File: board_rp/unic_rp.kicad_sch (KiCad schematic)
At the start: 193 parts, among them J1 SM03B-SRSS-TB, P1 USB_C_Plug_USB2.0, Q1 2N7002, Q10 2N7002, Q11 2N7002, Q12 2N7002, Q13 2N7002, Q14 2N7002, Q15 2N7002, Q16 2N7002, Q17 2N7002, Q18 2N7002, Q19 2N7002, Q2 2N7002, Q20 2N7002, Q21 2N7002, Q22 2N7002, Q23 2N7002, Q24 2N7002, Q25 2N7002, Q26 2N7002, Q27 2N7002, Q28 2N7002, Q29 2N7002, Q3 2N7002, Q30 2N7002, Q31 2N7002, Q32 2N7002, Q33 2N7002, Q34 2N7002, Q35 2N7002, Q36 2N7002, Q37 2N7002, Q38 2N7002, Q39 2N7002, Q4 2N7002, Q40 2N7002, Q41 2N7002, Q5 2N7002, Q6 2N7002, Q7 2N7002, Q8 2N7002, Q9 2N7002, U1 RP2350_80QFN, U3 MIC5203-3.3BM5, U4 APS6404L-3SQR-ZR, U6 AP62150Z6, U7 W25Q16JVUXIQ, X1 27MHz

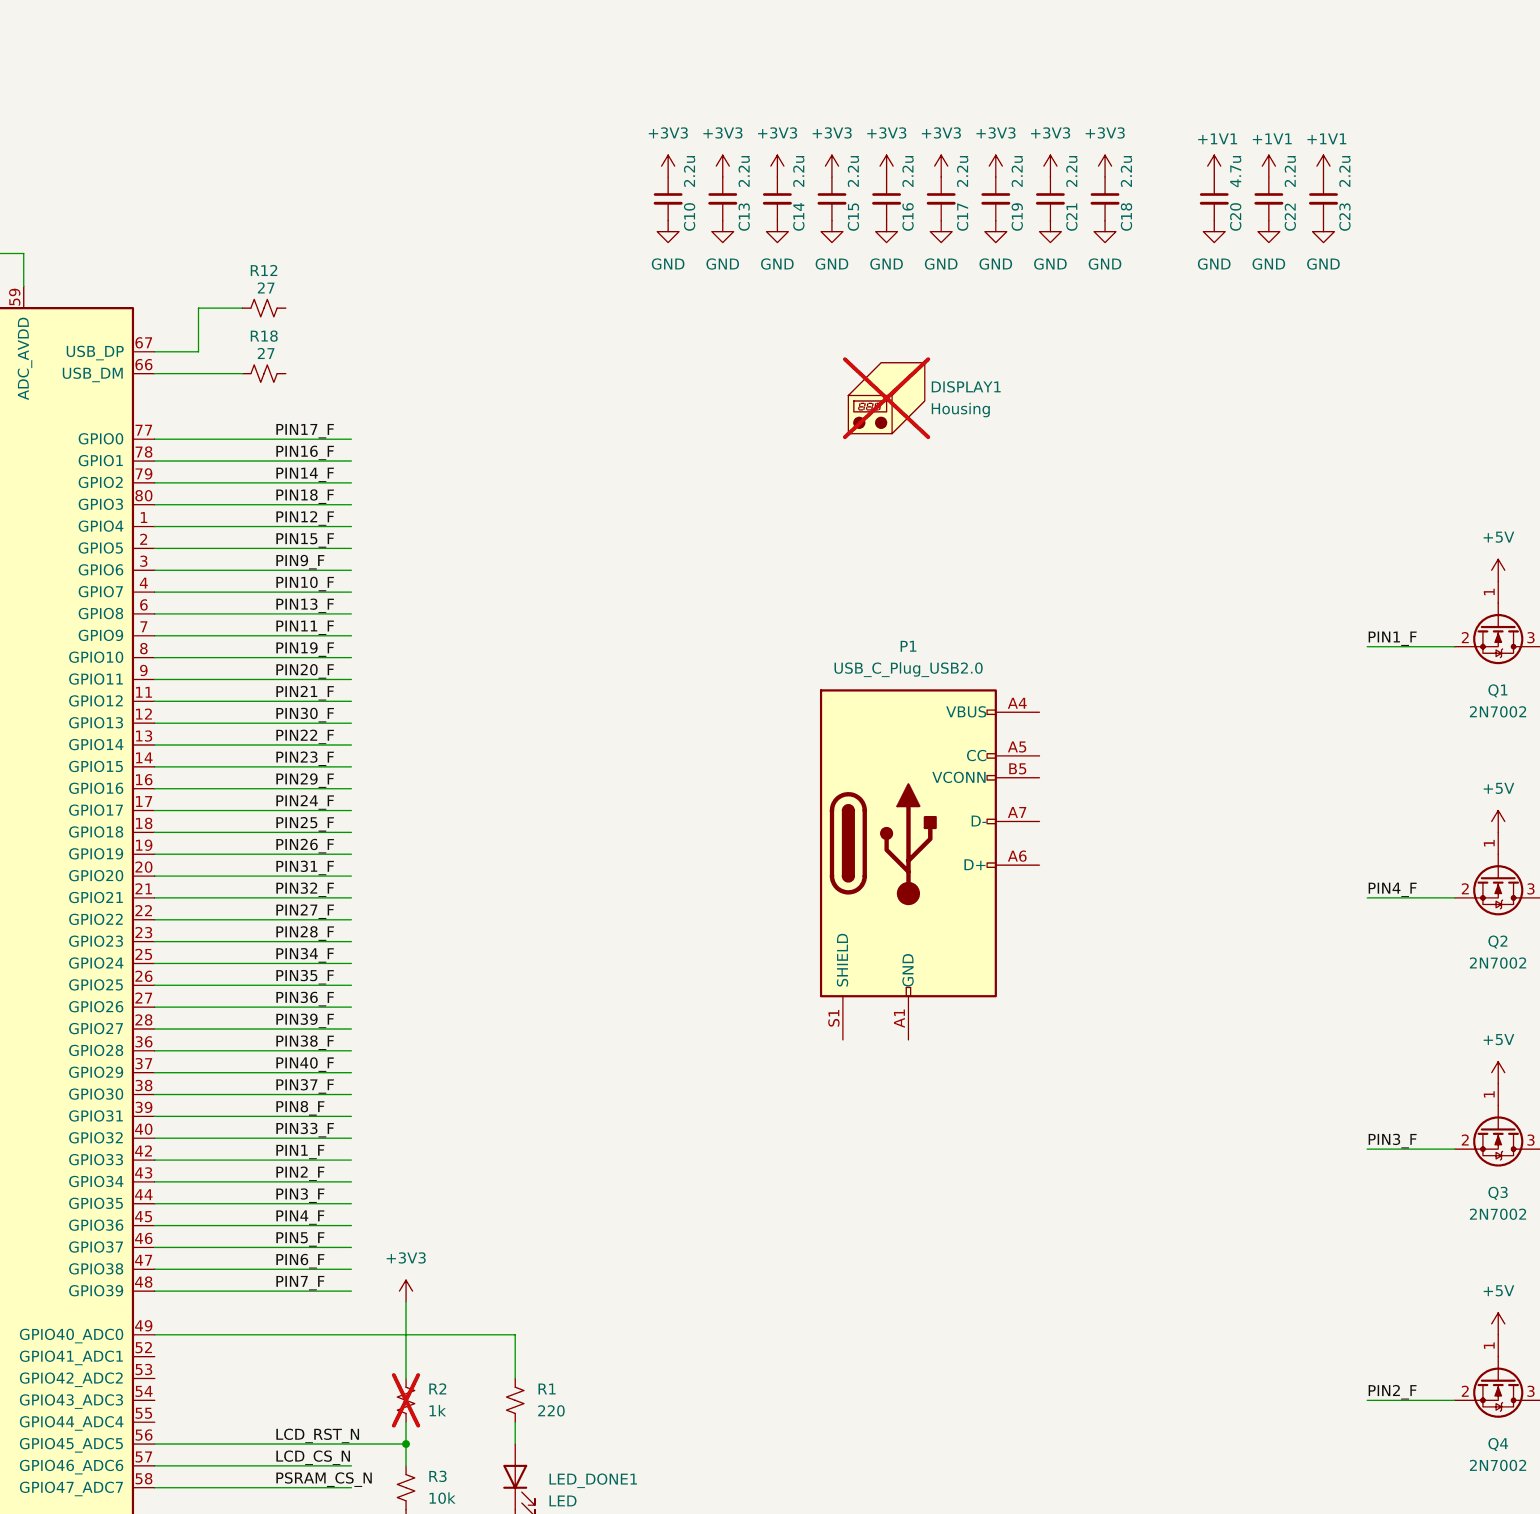
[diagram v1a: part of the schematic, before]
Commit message: More work towards UnIC-RP. This time power supplies are cleaned up a bit.
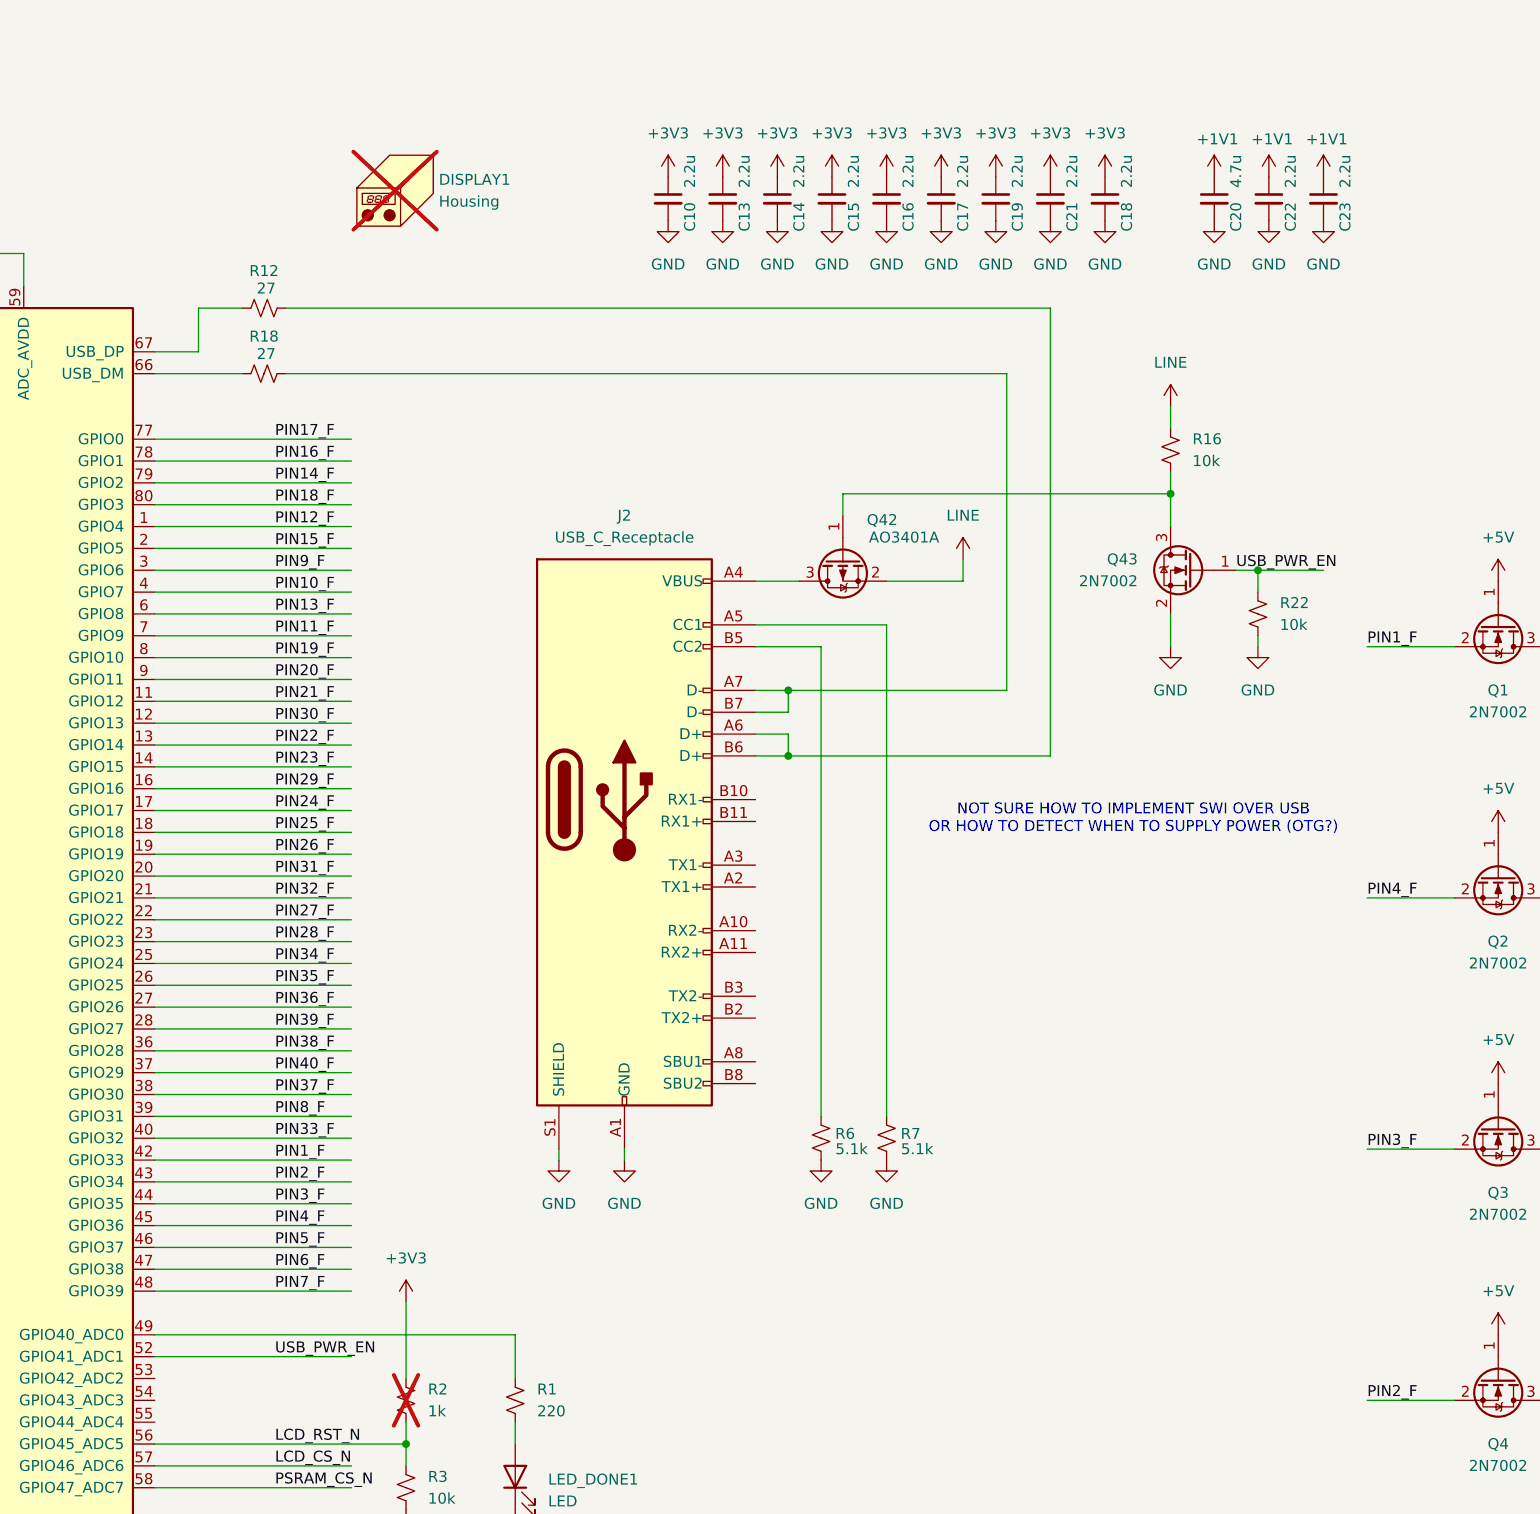
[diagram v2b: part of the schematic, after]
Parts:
- removed P1: USB_C_Plug_USB2.0, Connector_USB:USB_C_Receptacle_GCT_USB4115-03-C, symbol Connector:USB_C_Plug_USB2.0
- added J2: USB_C_Receptacle, Connector_USB:USB_C_Receptacle_GCT_USB4115-03-C, symbol Connector:USB_C_Receptacle
- added Q42: AO3401A, Package_TO_SOT_SMD:SOT-23, symbol Transistor_FET:AO3401A
- added Q43: 2N7002, UNIC:SOT-883, symbol Transistor_FET:2N7002
- added R16, R22: 10k, UNIC:R_0402_1005Metric_Pad0.72x0.64mm_HandSolder, symbol Device:R_Small_US
- added R6, R7: 5.1k, UNIC:R_0402_1005Metric_Pad0.72x0.64mm_HandSolder, symbol Device:R_Small_US
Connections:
- net GND: now also J2.A1 (GND), J2.A12 (GND), J2.B1 (GND), J2.B12 (GND), J2.S1 (SHIELD), Q43.2 (S), R22.2, R6.1, R7.1
- net LINE: now also Q42.2 (S), R16.1
- net at R12.2: now also J2.A6 (D+), J2.B6 (D+)
- net USB_PWR_EN: now reaches U1.52 (GPIO41_ADC1)
- net USB_PWR_EN: now also Q43.1 (G), R22.1
- net at R18.2: now also J2.A7 (D-), J2.B7 (D-)
- new net: J2.A5 (CC1), R7.2
- new net: J2.B5 (CC2), R6.2
- new net: Q42.1 (G), Q43.3 (D), R16.2
- new net: J2.A4 (VBUS), J2.A9 (VBUS), J2.B4 (VBUS), J2.B9 (VBUS), Q42.3 (D)
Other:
- note added: "NOT SURE HOW TO IMPLEMENT SWI OVER USB OR HOW TO DETECT WHEN TO SUPPLY POWER (OTG?)"
- moved on the sheet: DISPLAY1

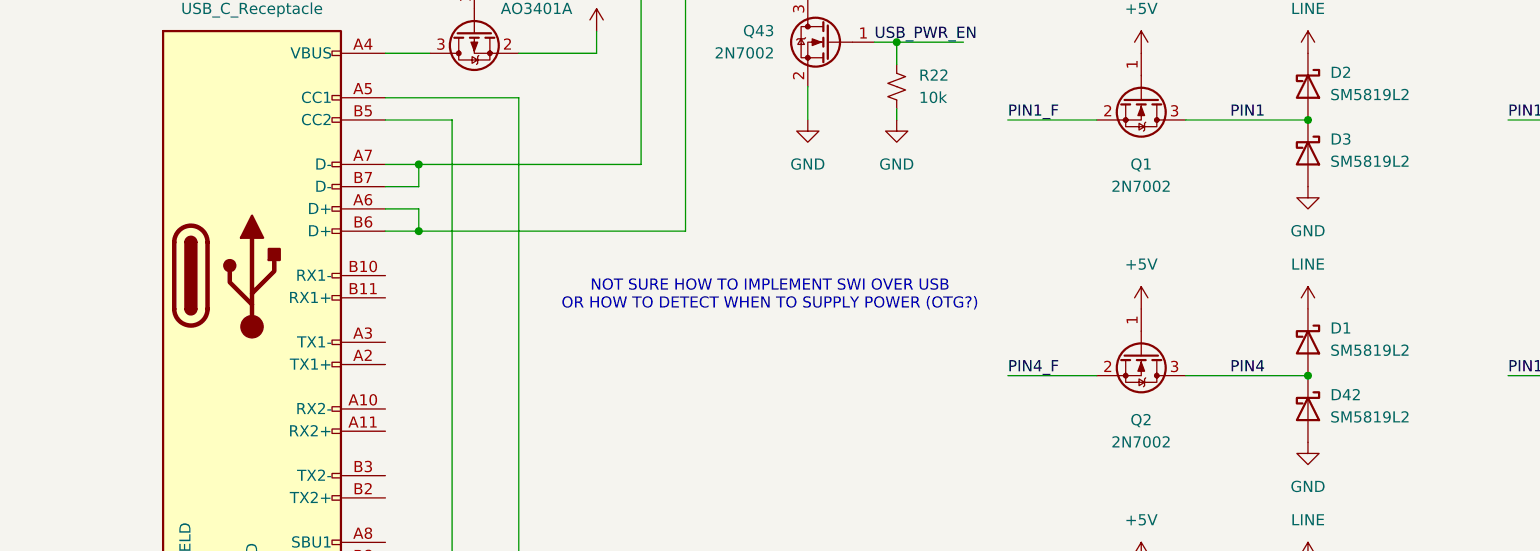
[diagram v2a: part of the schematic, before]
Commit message: Some notes about SWDBG over USB-C
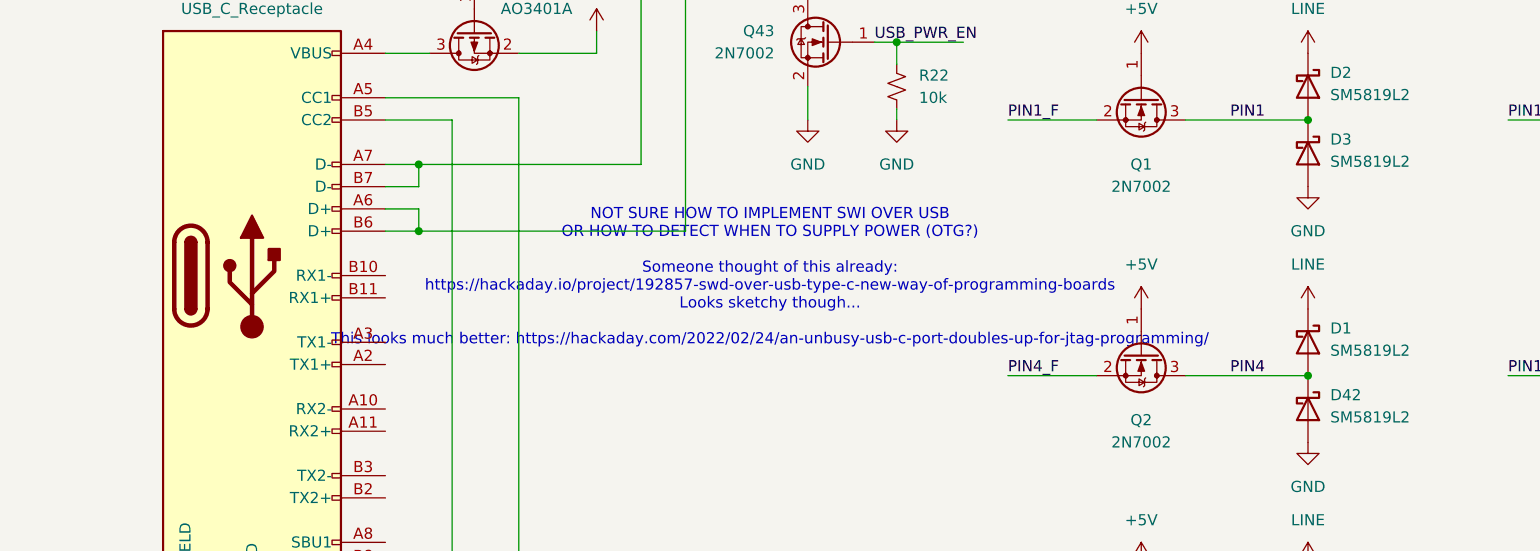
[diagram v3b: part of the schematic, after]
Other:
- note added: "NOT SURE HOW TO IMPLEMENT SWI OVER USB OR HOW TO DETECT WHEN TO SUPPLY POWER (OTG?) Someone thought of this already: https://hackaday.io/project/192857-swd-over-usb-type-c-new-way-of-programming-boards Looks sketchy though... This looks much better: https://hackaday.com/2022/02/24/an-unbusy-usb-c-port-doubles-up-for-jtag-programming/"
- note removed: "NOT SURE HOW TO IMPLEMENT SWI OVER USB OR HOW TO DETECT WHEN TO SUPPLY POWER (OTG?)"
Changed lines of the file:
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@@
 		)
 	)
-	(text "NOT SURE HOW TO IMPLEMENT SWI OVER USB\nOR HOW TO DETECT WHEN TO SUPPLY POWER (OTG?)\n"
+	(text "NOT SURE HOW TO IMPLEMENT SWI OVER USB\nOR HOW TO DETECT WHEN TO SUPPLY POWER (OTG?)\n\nSomeone thought of this already:\nhttps://hackaday.io/project/192857-swd-over-usb-type-c-new-way-of-programming-boards\nLooks sketchy though...\n\nThis looks much better: https://hackaday.com/2022/02/24/an-unbusy-usb-c-port-doubles-up-for-jtag-programming/\n\n\n"
 		(exclude_from_sim no)
 		(at 281.432 120.396 0)

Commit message: Much more complet RP schematic.
The USB-based debug setup is now drawn up. Component
placement is also complete. A thorough review is needed
especially on component footprints!
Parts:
- removed J1: SM03B-SRSS-TB, Connector_JST:JST_SH_SM03B-SRSS-TB_1x03-1MP_P1.00mm_Horizontal, symbol Connector_Generic_MountingPin:Conn_01x03_MountingPin
- added R23, R24: 10k, UNIC:R_0402_1005Metric_Pad0.72x0.64mm_HandSolder, symbol Device:R_Small_US
- added R25: 5.1k, UNIC:R_0402_1005Metric_Pad0.72x0.64mm_HandSolder, symbol Device:R_Small_US
- added R26: 68.k, UNIC:R_0402_1005Metric_Pad0.72x0.64mm_HandSolder, symbol Device:R_Small_US
- added U10, U2: ESD224DQA, Package_DFN_QFN:Diodes_UDFN-10_1.0x2.5mm_P0.5mm, symbol Power_Protection:ESD224DQA
- added U5: TMUX154ERSW, Package_DFN_QFN:UQFN-10_1.4x1.8mm_P0.4mm, symbol Analog_Switch:TMUX154ERSW
- added U8: LM393, Package_SON:WSON-8-1EP_3x2.5mm_P0.5mm_EP1.2x1.5mm_PullBack, symbol Comparator:LM393
- added U9: 74AUP1G08, Package_TO_SOT_SMD:SOT-353_SC-70-5, symbol 74xGxx:74AUP1G08
- J2: footprint Connector_USB:USB_C_Receptacle_GCT_USB4115-03-C -> UNIC:USB_C_Receptacle_GCT_USB4115-03-C
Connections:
- net +3V3: now also R23.1, R24.1, R26.2, U5.9 (VCC), U8.8 (V+), U9.5 (VCC)
- net GND: now also R25.1, U10.3 (VSS), U10.8 (VSS), U2.3 (VSS), U2.8 (VSS), U5.4 (GND), U5.8 (~{EN}), U8.4 (V-), U9.3 (GND)
- net SWCLK: now also U5.2 (A1)
- net SWD: now also U5.6 (B1)
- net USB_CC1: now reaches J2.A5 (CC1), R7.2
- net USB_CC1: now also U2.5, U8.3 (+)
- net USB_DP: now reaches J2.A6 (D+), J2.B6 (D+), R12.2
- net USB_DP: now also U10.2
- net USB_CC2: now reaches J2.B5 (CC2), R6.2
- net USB_CC2: now also U10.1, U8.5 (+)
- net USB_TXM: now reaches J2.A2 (TX1+)
- net USB_TXM: now also J2.B2 (TX2+), U2.1, U5.5 (B)
- net USB_TXP: now reaches J2.A3 (TX1-)
- net USB_TXP: now also J2.B3 (TX2-), U2.2, U5.3 (A)
- net VBUS: now reaches J2.A4 (VBUS), J2.A9 (VBUS), J2.B4 (VBUS), J2.B9 (VBUS), Q42.3 (D)
- net VBUS: now also U2.4
- net USB_DM: now reaches J2.A7 (D-), J2.B7 (D-), R18.2
- net USB_DM: now also U10.4
- new net: U5.10 (SEL), U9.4
- new net: R24.2, U8.1, U9.2
- new net: R25.2, R26.1, U8.2 (-), U8.6 (-)
- new net: R23.2, U8.7, U9.1
- no-connect marks 3 -> 17
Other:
- note added: "NOT SURE HOW TO IMPLEMENT SWI OVER USB OR HOW TO DETECT WHEN TO SUPPLY POWER (OTG?) Someone thought of this already: https://hackaday.io/project/192857-swd-over-usb-type-c-new-way-of-programming-boards Looks sketchy though... This looks much better: https://hackaday.com/2022/02/24/an-unbusy-usb-c-port-doubles-up-for-jtag-programming/ Probably best: https://github.com/minoseigenheer/SWD-over-USB-C"
- note removed: "NOT SURE HOW TO IMPLEMENT SWI OVER USB OR HOW TO DETECT WHEN TO SUPPLY POWER (OTG?) Someone thought of this already: https://hackaday.io/project/192857-swd-over-usb-type-c-new-way-of-programming-boards Looks sketchy though... This looks much better: https://hackaday.com/2022/02/24/an-unbusy-usb-c-port-doubles-up-for-jtag-programming/"
- moved on the sheet: C1, C12, C24, C26, C3, C5, C6, C7, C8, DISPLAY1, J2, L1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
